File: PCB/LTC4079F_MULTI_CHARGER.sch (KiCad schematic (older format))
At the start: 10 parts

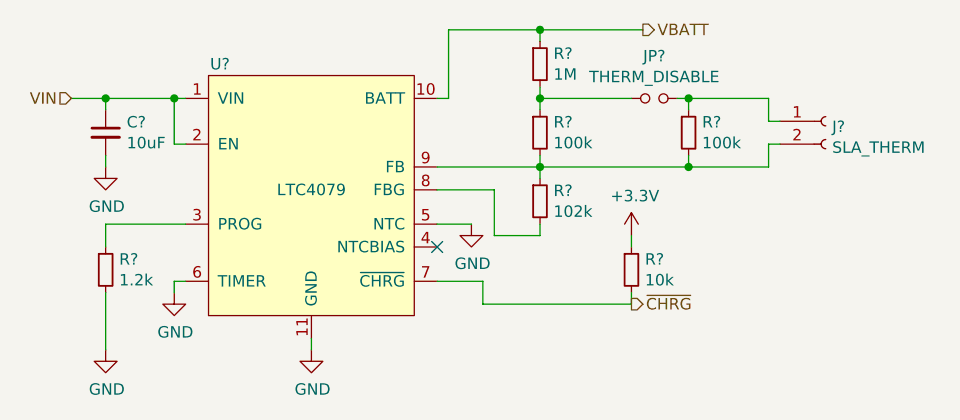
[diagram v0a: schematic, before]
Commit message: Simplified power supply
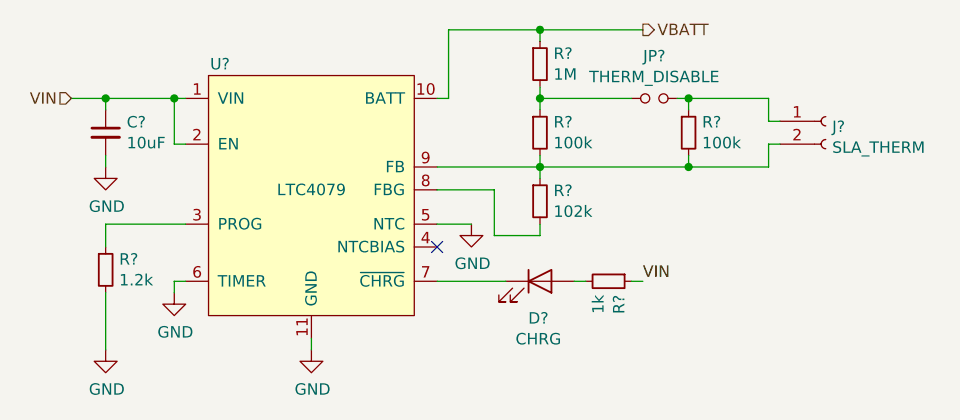
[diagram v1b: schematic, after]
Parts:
- added D?: CHRG, symbol Device:LED
- R?: value 10k -> 1k; Functional Block SLA Charger -> (none); SKU RES-0603-0004 -> (none); Solar Module Y -> (none)
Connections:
- net +3V3 is gone; now on net VIN: R?.1
- net ~CHRG: no longer names the net of U?.7 (~CHRG)
- net ~CHRG: now also D?.1 (K); no longer R?.2
- new net: D?.2 (A), R?.2
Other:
- moved on the sheet: R?
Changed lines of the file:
@@
 Text HLabel 4800 2500 2    50   Output ~ 0
 VBATT
-Text HLabel 4750 3700 2    50   Output ~ 0
-~CHRG
 $Comp
 L custom:LTC4079 U?
@@
 L Device:R_Small R?
 U 1 1 5C53CA2E
-P 4750 3550
-F 0 "R?" H 4809 3596 50  0000 L CNN
-F 1 "10k" H 4809 3505 50  0000 L CNN
-F 2 "Resistors:0603" H 4750 3550 50  0001 C CNN
-F 3 "~" H 4750 3550 50  0001 C CNN
-F 4 "SLA Charger" H 0   0   50  0001 C CNN "Functional Block"
-F 5 "RES-0603-0004" H 0   0   50  0001 C CNN "SKU"
-F 6 "Y" H 0   0   50  0001 C CNN "Solar Module"
-	1    4750 3550
-	1    0    0    -1
-$EndComp
-$Comp
-L power:+3.3V #PWR?
-U 1 1 5C53CADE
-P 4750 3400
-F 0 "#PWR?" H 4750 3250 50  0001 C CNN
-F 1 "+3.3V" H 4765 3573 50  0000 C CNN
-F 2 "" H 4750 3400 50  0001 C CNN
-F 3 "" H 4750 3400 50  0001 C CNN
-	1    4750 3400
-	1    0    0    -1
-$EndComp
-Wire Wire Line
-	4750 3400 4750 3450
-Wire Wire Line
-	4750 3700 4750 3650
-Wire Wire Line
-	3900 3600 4100 3600
-Wire Wire Line
-	4100 3600 4100 3700
-Wire Wire Line
-	4100 3700 4750 3700
+P 4650 3600
+F 0 "R?" H 4709 3646 50  0000 L CNN
+F 1 "1k" H 4709 3555 50  0000 L CNN
+F 2 "Resistors:0603" H 4650 3600 50  0001 C CNN
+F 3 "~" H 4650 3600 50  0001 C CNN
+	1    4650 3600
+	0    1    1    0
+$EndComp
+Wire Wire Line
+	4800 3600 4750 3600
+Wire Wire Line
+	4500 3600 4550 3600
 Wire Wire Line
 	2300 2800 2450 2800
@@
 	5350 3100 5000 3100
 Connection ~ 5000 3100
+$Comp
+L Device:LED D?
+U 1 1 5E970504
+P 4350 3600
+F 0 "D?" H 4343 3438 50  0000 C CNN
+F 1 "CHRG" H 4343 3347 50  0000 C CNN
+F 2 "" H 4350 3600 50  0001 C CNN
+F 3 "~" H 4350 3600 50  0001 C CNN
+	1    4350 3600
+	1    0    0    -1
+$EndComp
+Wire Wire Line
+	3900 3600 4200 3600
+Text Label 4800 3600 0    50   ~ 0
+VIN
 $EndSCHEMATC
